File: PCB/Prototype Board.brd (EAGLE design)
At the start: 55.9 x 76.2 mm, 65 parts, among them J1 USB Type C, J3 Connector, J4 Battery Connector, Q1 S8050, Q10 20V/0.2A/8MHz/1.2Ω/1Vth, Q12 20V/0.2A/8MHz/1.2Ω/1Vth, Q14 20V/0.2A/8MHz/1.2Ω/1Vth, Q16 20V/0.2A/8MHz/1.2Ω/1Vth, Q3 20V/4.2A/52mΩ/1.4W, Q4 S8050, Q6 20V/0.2A/8MHz/1.2Ω/1Vth, Q8 20V/0.2A/8MHz/1.2Ω/1Vth, U1 9DoF IMU, U2 MCP73831, U3 ESP-WROOM-32, U5 DWM1000, U6 1.8V/100mA, U7 CH340C, U8 XC6222B331MR-G

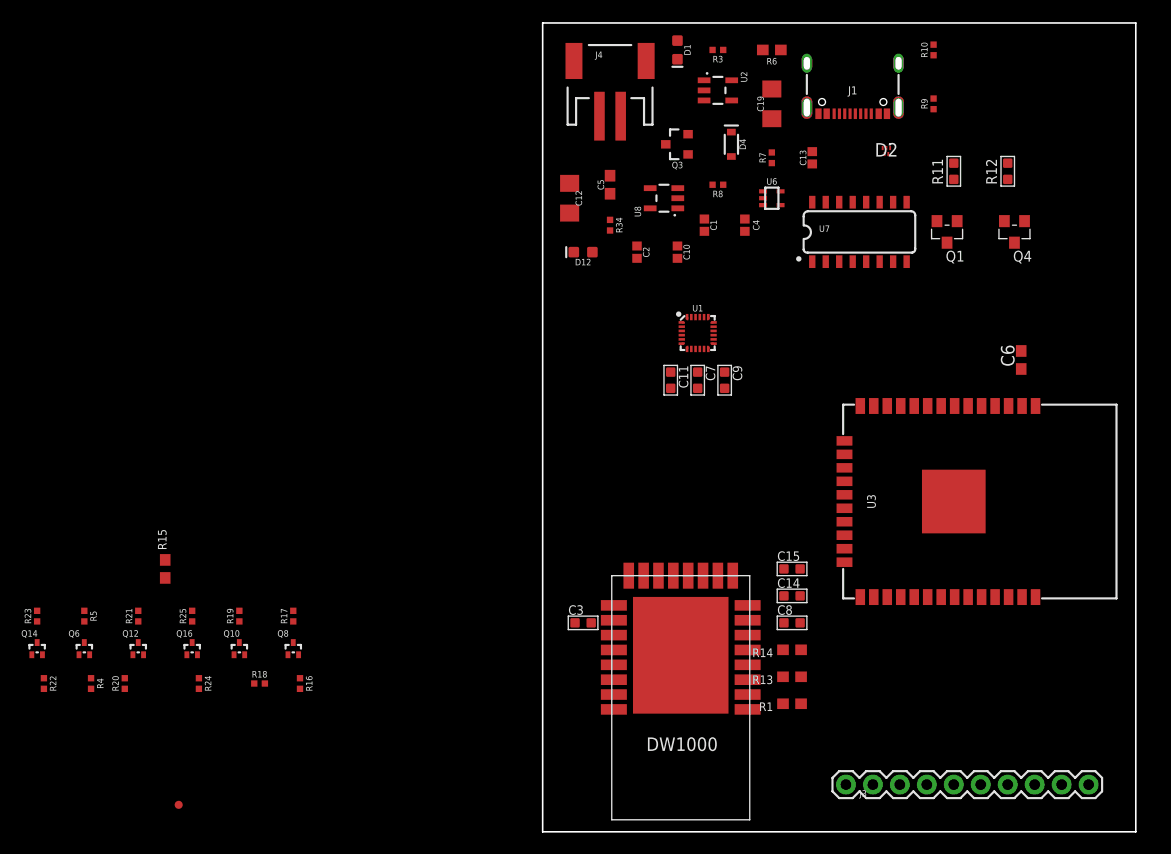
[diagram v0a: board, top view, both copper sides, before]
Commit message: Grouped Schematic
Components selected, laid out, not routed yet
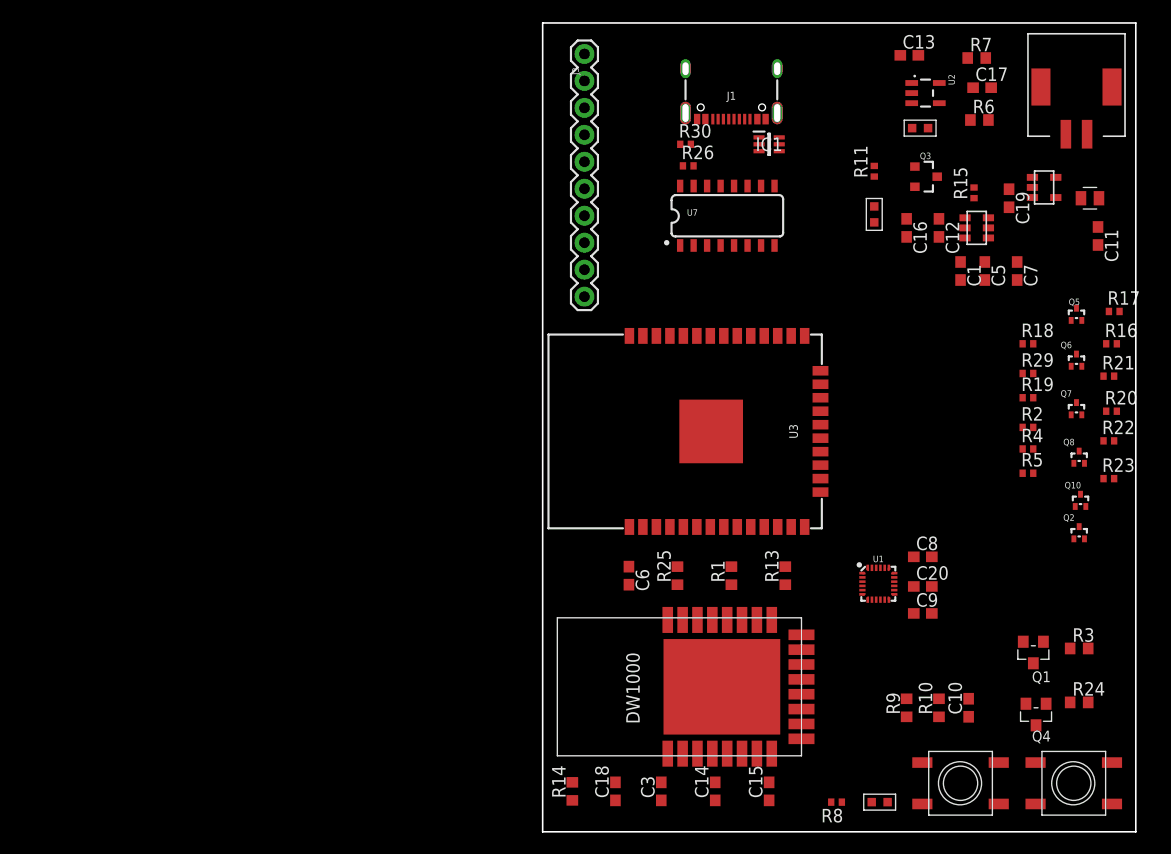
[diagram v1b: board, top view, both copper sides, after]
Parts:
- removed C2: 0.1uF, SparkFun-Capacitors:0402
- removed C4: 1.0uF, SparkFun-Capacitors:0402
- removed D1: Yellow, SparkFun-LED:LED-0603
- removed D12: RED, SparkFun-LED:LED-0603
- removed D2: RCLAMP7522T.TNT, RCLAMP7522T.TNT:RCLAMP7522TTNT
- removed D4: 3A/10V/280mV, SparkFun-DiscreteSemi:SOD-323
- removed J4: Battery Connector, SparkFun-Connectors:JST-2-SMD
- removed Q12, Q14, Q16: 20V/0.2A/8MHz/1.2Ω/1Vth, SparkFun-DiscreteSemi:SOT-416FL
- removed R12: 1K, Discrete:0603
- removed R34: 1k, SparkFun-Resistors:0402-TIGHT
- removed TP1: 1.8V, SparkFun-Connectors:PAD.03X.03
- removed U6: 1.8V/100mA, SparkFun-IC-Power:SC70
- removed U8: XC6222B331MR-G, SparkFun-IC-Power:SOT23-5
- added C16: C_2.2UF/16V_0603, JLC PCB Basic Parts_loc:C0603
- added C17: C_4.7UF/16V_0603, JLC PCB Basic Parts_loc:C0603
- added C18: C_10UF/25V_0603, JLC PCB Basic Parts_loc:C0603
- added C20: C_100NF/50V_0603, JLC PCB Basic Parts_loc:C0603
- added IC1: SMF05CT1G, SMF05CT1G:SOT65P210X110-6N
- added Q2, Q5, Q7: 20V/0.2A/8MHz/1.2Ω/1Vth, SparkFun-DiscreteSemi:SOT-416FL
- added R2, R29: R_2.2K_0402, JLC PCB Basic Parts_loc:R0402
- added R26, R30: R_5.1K_0402, JLC PCB Basic Parts_loc:R0402
- added U$1, U$3: K2-6639SP-C4SC-04_C83206, customlib:K2-6639SP-C4SC-04
- added U$2: MLF2012, customlib:MLF2012
- added U$4: TPS62202DBVR, customlib:TPS62202DBVR
- added U$5: HE9008M6R, customlib:HE9008M6R
- added U$6, U$7, U$9: 19-217/GHC-YR1S2/3T, customlib:19-217/GHC-YR1S2/3T
- added U$8: SM02B_PASS_TB_LF, customlib:SM02B_PASS_TB_LF
- C1: value 1.0uF -> C_2.2UF/16V_0603; device SparkFun-Capacitors:0402 -> JLC PCB Basic Parts_loc:C0603
- C10: value 1.0uF -> C_100NF/50V_0603; device SparkFun-Capacitors:0402 -> JLC PCB Basic Parts_loc:C0603
- C11: value 0.1uF -> C_10UF/10V_0603; device Discrete:C0603 -> JLC PCB Basic Parts_loc:C0603
- C12: value 4.7uF -> C_2.2UF/16V_0603; device SparkFun-Capacitors:1206 -> JLC PCB Basic Parts_loc:C0603
- C13: value 0.1uF -> C_4.7UF/16V_0603; device SparkFun-Capacitors:0402 -> JLC PCB Basic Parts_loc:C0603
- C14, C15, C3: value 0.1uF -> C_100NF/50V_0603; device Discrete:C0603 -> JLC PCB Basic Parts_loc:C0603
- C19: value 4.7uF -> C_4.7UF/16V_0603; device SparkFun-Capacitors:1206 -> JLC PCB Basic Parts_loc:C0603
- C5: value 10uF -> C_2.2UF/16V_0603; device SparkFun-Capacitors:0603 -> JLC PCB Basic Parts_loc:C0603
- C6: value 10uF -> C_10UF/25V_0603; device rcl:C0603 -> JLC PCB Basic Parts_loc:C0603
- C7: value 1.0uF -> C_100NF/50V_0603; device Discrete:C0603 -> JLC PCB Basic Parts_loc:C0603
- C8: value 10uF -> C_100NF/50V_0603; device Discrete:C0603 -> JLC PCB Basic Parts_loc:C0603
- C9: value 0.1uF -> C_1UF/50V_0603; device Discrete:C0603 -> JLC PCB Basic Parts_loc:C0603
- R1, R13: value 1K -> R_1K_0603; device microbuilder:0603-NO -> JLC PCB Basic Parts_loc:R0603
- R10, R9: value 5.1k -> R_10K_0603; device SparkFun-Resistors:0402-TIGHT -> JLC PCB Basic Parts_loc:R0603
- R11: value 1K -> R_10K_0402; device Discrete:0603 -> JLC PCB Basic Parts_loc:R0402
- R14: value 1K -> R_10K_0603; device microbuilder:0603-NO -> JLC PCB Basic Parts_loc:R0603
- R15: value 10K -> R_10K_0402; device microbuilder:0603-NO -> JLC PCB Basic Parts_loc:R0402
- R16, R17, R18, R19, R20, R21, R22, R23, R4, R5: value 2.2k -> R_2.2K_0402; device SparkFun-Resistors:0402-TIGHT -> JLC PCB Basic Parts_loc:R0402
- R24, R25: value 2.2k -> R_1K_0603; device SparkFun-Resistors:0402-TIGHT -> JLC PCB Basic Parts_loc:R0603
- R3: value 1k -> R_1K_0603; device SparkFun-Resistors:0402-TIGHT -> JLC PCB Basic Parts_loc:R0603
- R6: value 2.0k -> R_2K_0603; device SparkFun-Resistors:0603 -> JLC PCB Basic Parts_loc:R0603
- R7: value 10k -> R_4.7K_0603; device SparkFun-Resistors:0402-TIGHT -> JLC PCB Basic Parts_loc:R0603
- R8: value 10k -> R_1K_0402; device SparkFun-Resistors:0402-TIGHT -> JLC PCB Basic Parts_loc:R0402
- moved R22 102.9 mm to (53.3, 36.8), turned to 0 degrees
- moved R23 101.8 mm to (53.3, 33.3), turned to 0 degrees
- moved Q6 97.3 mm to (50.3, 45.0)
- moved R20 96.4 mm to (53.6, 39.6), turned to 0 degrees
- moved R21 94.2 mm to (53.3, 42.9), turned to 0 degrees
- moved R4 91.0 mm to (45.7, 36.1), turned to 0 degrees
- moved R5 89.9 mm to (45.7, 33.8), turned to 0 degrees
- moved R15 84.0 mm to (40.6, 60.2)
- moved R24 83.0 mm to (50.5, 12.2), turned to 0 degrees
- moved R16 82.9 mm to (53.6, 46.0), turned to 0 degrees
- moved R17 82.5 mm to (53.8, 49.0), turned to 0 degrees
- moved Q10 80.5 mm to (50.7, 31.8)
- moved R18 79.1 mm to (45.7, 46.0)
- moved R19 77.1 mm to (45.7, 40.9), turned to 0 degrees
- moved Q8 76.2 mm to (50.5, 35.8)
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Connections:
- removed net N$30: D12.A, R34.2
- removed net TP_EN: R8.2, U8.3
- new net N$15: C12.2, U$5.C+
- new net N$4: R8.1, U$9.1
- new net N$8: U$2.1, U$4.4, U$4.5
- new net N$9: R15.2, U$5.EN
- net +3V3: now also R10.1, R9.1
- net 1.8V: now also C20.1, C9.1, Q2.1, Q5.1, Q7.1, R20.2, R29.2, U$2.2; no longer C13.1, C7.1, Q14.1, Q16.1, R24.2, TP1.P$1, U6.5
- net 3.3V: now also C1.1, C18.1, C7.1, R2.2, R8.2, U$5.VOUT; no longer C10.1, C2.1, C8.1, R25.2, R34.1, U8.5
- net CHG_LED: now also R7.1, U$6.1; no longer D1.A, R3.2
- net D+: now also IC1.3; no longer D2.3
- net D-: now also IC1.6; no longer D2.4
- net DTR: now also R24.1; no longer R12.2
- net FSYNC/IO33: now also Q7.2, R20.1; no longer Q14.2, R22.1
- net GND: now also C16.2, C17.2, C18.2, C20.2, IC1.2, R11.1, R14.1, R26.1, R30.1, U$1.P3, U$1.P4, U$3.P3, U$3.P4, U$4.2, U$5.GND, U$8.3, U$9.2; no longer C12.2, C2.2, C4.2, D12.C, D2.5, J4.1, R10.1, R15.2, R7.1, R9.1, U6.2, U8.2
- net GPIO12: now also Q2.3, R19.1; no longer Q12.3, R21.1
- net GPIO12/SDO: now also Q2.2, R18.1; no longer Q12.2, R20.1
- net GPIO13: now also Q5.3; no longer Q8.3
- net GPIO13/SDI: now also Q5.2; no longer Q8.2
- net GPIO15: now also R2.1; no longer R19.1
- net GPIO15/CS: now also R29.1; no longer R18.1
- net INT/IO34: now also Q8.2, R22.1; no longer Q16.2, R24.1
- net IO0: now also R9.2, U$3.P1, U$3.P2
- net IO27: now also R13.2; no longer R14.1
- net IO32: now also R25.2; no longer R13.1
- net IO33: now also Q7.3, R1.2, R21.1; no longer Q14.3, R1.1, R23.1
- net IO34: now also Q8.3, R14.2, R23.1; no longer Q16.3, R15.1, R25.1
- net N$1: now also R24.2; no longer R12.1
- net N$10: now also R1.1; no longer R1.2
- net N$11: now also R25.1; no longer R13.2
- net N$12: now also R13.1; no longer R14.2
- net N$13: now also C8.1; no longer C9.1
- net N$14: now also C12.1, U$5.C-; no longer Q1.1, R11.1
- net N$2: now also Q1.1, R3.2; no longer Q12.1, R20.2
- net N$5: now also R26.2; no longer R9.2
- net N$6: now also R30.2; no longer R10.2
- net N$7: now also U$6.2; no longer D1.C
- net RESET: now also C10.1, R10.2, U$1.P1, U$1.P2
- net RTS: now also R3.1; no longer R11.2
- net V_BATT: now also C17.1, U$8.4; no longer C12.1, J4.2
- net V_IN: now also C16.1, C19.1, R15.1, U$4.1, U$4.3, U$5.VIN, U$7.2; no longer C1.1, C4.1, D4.C, R8.1, U6.1, U6.3, U8.1
- net V_USB: now also C13.1, IC1.1, R11.2, U$7.1; no longer C19.1, D2.1, D4.A, R3.1
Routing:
- added copper zone on layer 15, net GND
- added copper zone on layer 2, net GND

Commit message: Board Almost Finished
Need to route IO connectors, retouch design rules, clean up connections, etc
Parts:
- moved J3 68.3 mm to (52.9, 25.7)
- moved U$9 54.2 mm to (20.8, 55.8), turned to 180 degrees
- moved R8 53.7 mm to (23.6, 56.3), turned to 90 degrees
- moved Q10 49.2 mm to (3.19, 44.5), turned to 90 degrees
- moved Q6 47.2 mm to (3.22, 40.9), turned to 90 degrees
- moved R16 46.2 mm to (7.79, 39.8)
- moved R23 46.2 mm to (10.5, 50.4), turned to 180 degrees
- moved R17 46.0 mm to (9.44, 37.0), turned to 270 degrees
- moved C6 45.8 mm to (45.1, 51.2), turned to 0 degrees
- moved Q5 44.1 mm to (7.79, 37.5), turned to 180 degrees
- moved R22 43.3 mm to (11.1, 46.3), turned to 180 degrees
- moved R2 42.8 mm to (3.78, 46.4)
- moved R5 42.4 mm to (3.68, 38.9)
- moved Q8 41.6 mm to (11.1, 48.9)
- moved R20 41.1 mm to (12.9, 45.5), turned to 90 degrees
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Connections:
- net D+ renamed D_P
- net D- renamed D_N
- net FSYNC/IO33 renamed FSYNC/IO36
- net INT/IO34 renamed INT/IO39
- net RX renamed RX-TX_P
- net TX renamed RX-TX_N
- removed net +3V3: C6.1, R10.1, R9.1, U3.2
- net 3.3V: now also C6.1, R10.1, R9.1, U3.2
- net GND: now also U5.VSS.5
- net IO16: no longer J3.3
- net IO17: no longer J3.4
- net IO2: no longer J3.1
- net IO21: no longer J3.5
- net IO22: no longer J3.6
- net IO25: no longer J3.7
- net IO26: no longer J3.8
- net IO33: no longer Q7.3, R21.1
- net IO34: no longer Q8.3, R23.1
- net IO36: now also Q7.3, R21.1; no longer J3.9
- net IO39: now also Q8.3, R23.1; no longer J3.10
- net IO4: no longer J3.2
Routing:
- net 3.3V: track 0.00 -> 188.2 mm, vias 0 -> 8
- net GND: track 0.00 -> 99.9 mm, vias 0 -> 21
- net 1.8V: track 0.00 -> 88.3 mm, vias 0 -> 7
- net IO33: track 0.00 -> 69.8 mm, vias 0 -> 2
- net IO32: track 0.00 -> 67.8 mm, vias 0 -> 2
- net RTS: track 0.00 -> 66.3 mm, vias 0 -> 4
- net GPIO35: track 0.00 -> 65.7 mm, vias 0 -> 4
- net DTR: track 0.00 -> 60.7 mm, vias 0 -> 2
- net IO27: track 0.00 -> 56.9 mm, vias 0 -> 2
- net RX-TX_P: track 0.00 -> 56.5 mm, vias 0 -> 2
- net RX-TX_N: track 0.00 -> 55.9 mm, vias 0 -> 2
- net IO34: track 0.00 -> 51.2 mm, vias 0 -> 2
- net GPIO14: track 0.00 -> 43.1 mm, vias 0 -> 2
- net GPIO15: track 0.00 -> 39.7 mm
- net IO39: track 0.00 -> 37.9 mm, vias 0 -> 2
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
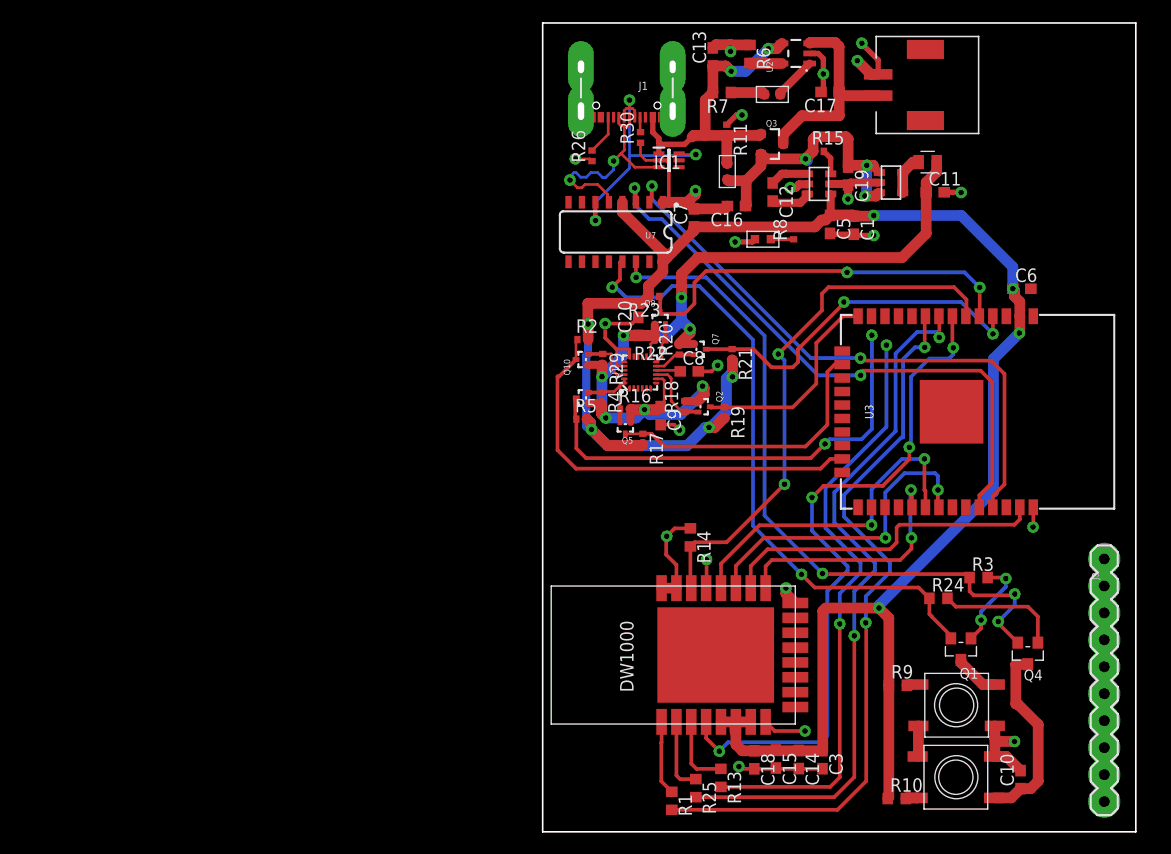
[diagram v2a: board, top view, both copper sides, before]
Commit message: Resolved half of the warnings
Will need to look into the USB footprint. Looks odd
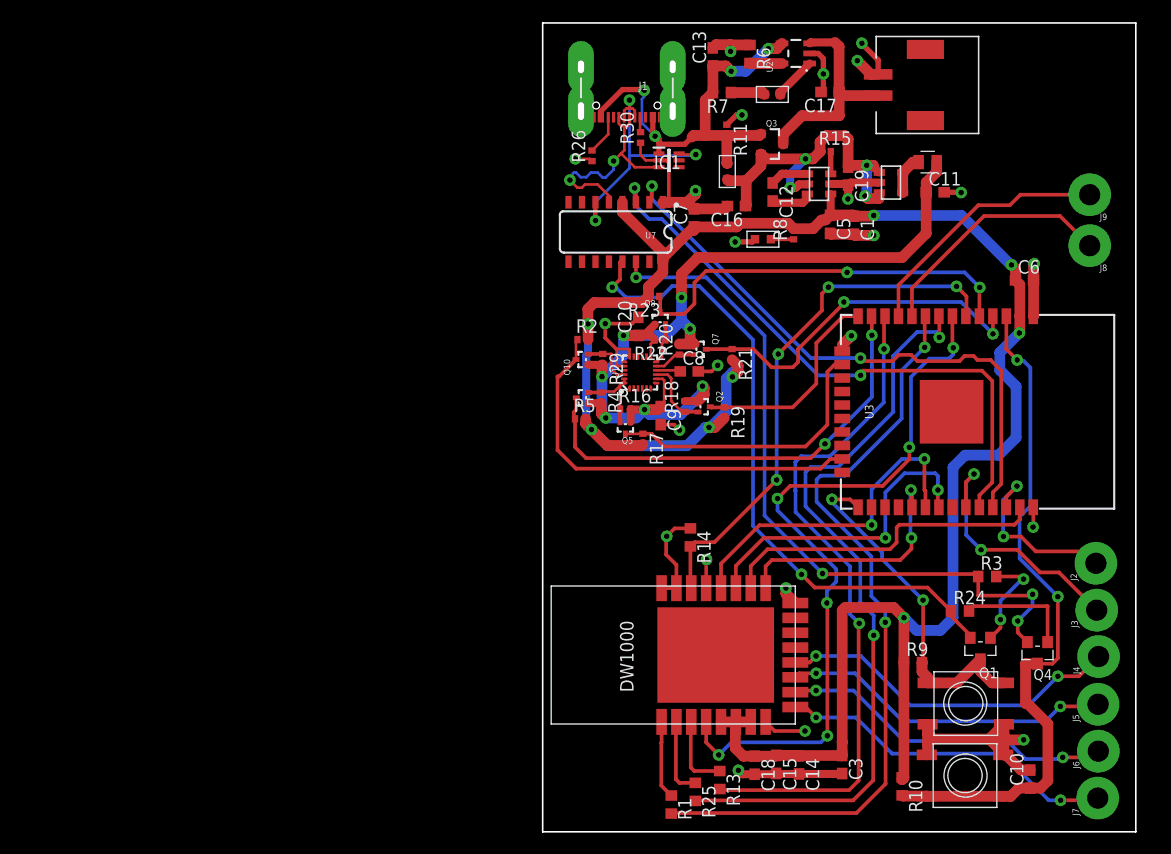
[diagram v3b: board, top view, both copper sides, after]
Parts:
- added J2, J4, J5, J6, J7, J8, J9: (no value), SparkFun-Connectors:1X01_2MM
- J3: value Connector -> (none); device SparkFun-Connectors:1X10 -> SparkFun-Connectors:1X01_2MM
- moved J3 4.88 mm to (52.2, 20.9), turned to 90 degrees
- moved R9 2.56 mm to (34.9, 15.9)
- moved R24 2.36 mm to (39.3, 20.8)
- moved C3 1.91 mm to (28.2, 6.34)
- moved Q1 1.83 mm to (41.2, 17.3)
- moved R10 1.25 mm to (33.9, 4.28), turned to 270 degrees
- moved C10 0.92 mm to (45.9, 4.96)
- moved Q4 0.92 mm to (46.6, 16.9)
- moved U$3 0.88 mm to (39.9, 12.1)
- moved U$1 0.88 mm to (39.8, 5.30)
- moved C6 0.83 mm to (45.4, 52.0)
- moved R3 0.82 mm to (41.9, 24.1)
- moved R15 0.66 mm to (26.6, 64.1)
- moved C14 0.51 mm to (24.2, 6.30)
- moved C15 0.51 mm to (22.0, 6.35)
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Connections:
- new net DW3: J4.1, U5.GPIO3
- new net DW4: J5.1, U5.GPIO4
- new net DW5: J6.1, U5.GPIO5
- new net DW6: J7.1, U5.GPIO6
- net IO21: now also J3.1
- net IO22: now also J2.1
- net IO25: now also J8.1
- net IO26: now also J9.1
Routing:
- net RESET: track 19.1 -> 65.0 mm, vias 0 -> 2
- net DW3: track 0.00 -> 32.7 mm, vias 0 -> 2
- net DW6: track 0.00 -> 32.2 mm, vias 0 -> 2
- net DW5: track 0.00 -> 31.6 mm, vias 0 -> 2
- net DW4: track 0.00 -> 31.2 mm, vias 0 -> 2
- net IO0: track 4.37 -> 33.6 mm, vias 0 -> 2
- net GND: track 99.9 -> 126.1 mm, vias 21 -> 23
- net IO21: track 0.00 -> 24.7 mm, vias 0 -> 2
- net IO26: track 0.00 -> 24.5 mm
- net IO25: track 0.00 -> 23.4 mm
- net IO22: track 0.00 -> 17.5 mm, vias 0 -> 2
- net V_USB: track 33.7 -> 42.0 mm, vias 2 -> 4
- net 3.3V: track 188.2 -> 196.2 mm
- net IO27: track 56.9 -> 64.9 mm
- net IO32: track 67.8 -> 72.9 mm
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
